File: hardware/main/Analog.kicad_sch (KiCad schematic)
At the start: 61 parts, among them J301 Overvoltage_protection, J302 Rad_sensor, J303 Mos_temp, J304 Diode_temp, U301 INA823DT, U302 INA823DT, U303 INA293A4, U304 INA293A4, U305 TL7726IDR_1

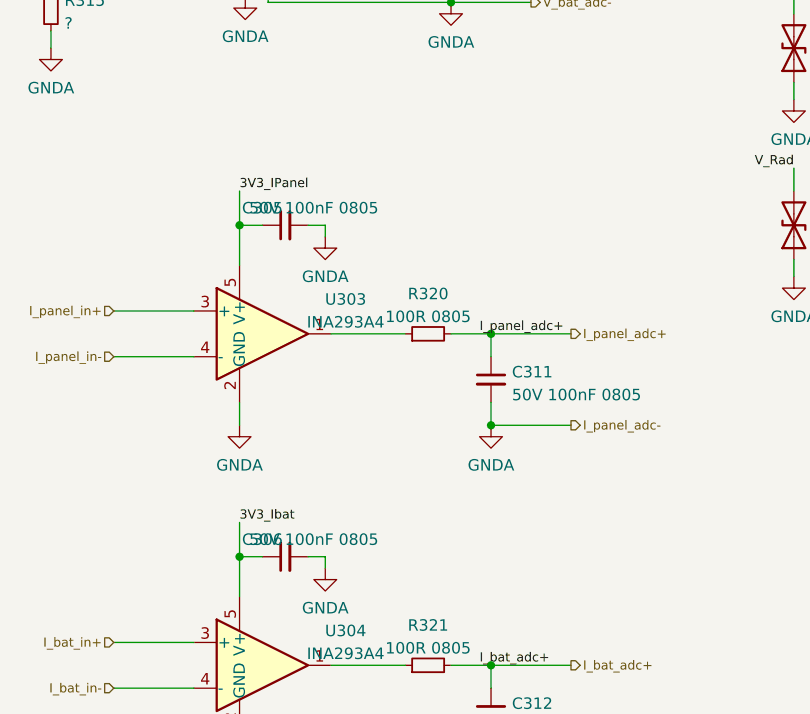
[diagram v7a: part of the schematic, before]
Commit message: Layout: Fist version of power stage
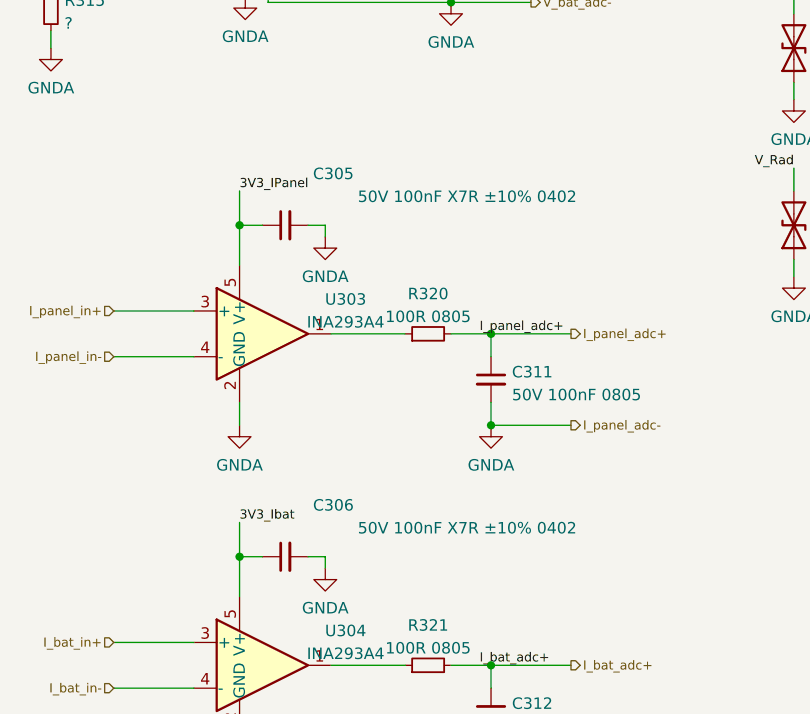
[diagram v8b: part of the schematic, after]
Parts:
- C305, C306: value 50V 100nF 0805 -> 50V 100nF X7R ±10% 0402; footprint Capacitor_SMD:C_0805_2012Metric_Pad1.18x1.45mm_HandSolder -> Capacitor_SMD:C_0402_1005Metric_Pad0.74x0.62mm_HandSolder
- JP301, JP302, JP303, JP304: footprint Jumper:SolderJumper-2_P1.3mm_Open_TrianglePad1.0x1.5mm -> Zenite:SolderJumper-2_P0.5mm_Open_TrianglePad0.5x0.5mm
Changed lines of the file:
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@@
+    (stroke (width 0) (type default) (color 0 0 0 0))
+  )
+  (wire (pts (xy 128.27 164.465) (xy 130.81 164.465))
     (stroke (width 0) (type default) (color 0 0 0 0))
   )
@@
   )
   (wire (pts (xy 135.89 164.465) (xy 137.795 164.465))
-    (stroke (width 0) (type default) (color 0 0 0 0))
-  )
-  (wire (pts (xy 128.27 164.465) (xy 130.81 164.465))
     (stroke (width 0) (type default) (color 0 0 0 0))
   )
@@
     )
     (property "Datasheet" "~" (id 3) (at 100.965 97.79 0)
+      (effects (font (size 1.27 1.27)) hide)
+    )
+    (pin "1")
+    (pin "2")
+  )
+  (symbol (lib_id "Device:C_Small") (at 133.35 127.635 90) (unit 1)
+    (in_bom yes) (on_board yes)
+    (property "Reference" "C305" (id 0) (at 140.97 121.92 90)
+      (effects (font (size 1.27 1.27)) (justify left))
+    )
+    (property "Value" "50V 100nF X7R ±10% 0402" (id 1) (at 165.735 124.46 90)
+      (effects (font (size 1.27 1.27)) (justify left))
+    )
+    (property "Footprint" "Capacitor_SMD:C_0402_1005Metric_Pad0.74x0.62mm_HandSolder" (id 2) (at 133.35 127.635 0)
+      (effects (font (size 1.27 1.27)) hide)
+    )
+    (property "Datasheet" "~" (id 3) (at 133.35 127.635 0)
       (effects (font (size 1.27 1.27)) hide)
     )
@@
     (property "Reference" "JP304" (id 0) (at 257.175 53.4502 0))
     (property "Value" "Disable_Ibat" (id 1) (at 257.175 55.9871 0))
-    (property "Footprint" "Jumper:SolderJumper-2_P1.3mm_Open_TrianglePad1.0x1.5mm" (id 2) (at 257.175 57.785 0)
+    (property "Footprint" "Zenite:SolderJumper-2_P0.5mm_Open_TrianglePad0.5x0.5mm" (id 2) (at 257.175 57.785 0)
       (effects (font (size 1.27 1.27)) hide)
     )
@@
     (pin "1")
   )
+  (symbol (lib_id "Device:C_Small") (at 133.35 164.465 90) (unit 1)
+    (in_bom yes) (on_board yes)
+    (property "Reference" "C306" (id 0) (at 140.97 158.75 90)
+      (effects (font (size 1.27 1.27)) (justify left))
+    )
+    (property "Value" "50V 100nF X7R ±10% 0402" (id 1) (at 165.735 161.29 90)
+      (effects (font (size 1.27 1.27)) (justify left))
+    )
+    (property "Footprint" "Capacitor_SMD:C_0402_1005Metric_Pad0.74x0.62mm_HandSolder" (id 2) (at 133.35 164.465 0)
+      (effects (font (size 1.27 1.27)) hide)
+    )
+    (property "Datasheet" "~" (id 3) (at 133.35 164.465 0)
+      (effects (font (size 1.27 1.27)) hide)
+    )
+    (pin "1")
+    (pin "2")
+  )
   (symbol (lib_id "power:GNDA") (at 107.315 68.58 0) (unit 1)
     (in_bom yes) (on_board yes) (fields_autoplaced)
@@
     )
     (property "Datasheet" "~" (id 3) (at 56.515 113.665 0)
-      (effects (font (size 1.27 1.27)) hide)
-    )
-    (pin "1")
-    (pin "2")
-  )
-  (symbol (lib_id "Device:C_Small") (at 133.35 127.635 90) (unit 1)
-    (in_bom yes) (on_board yes)
-    (property "Reference" "C305" (id 0) (at 130.81 125.73 90))
-    (property "Value" "50V 100nF 0805" (id 1) (at 136.525 125.73 90))
-    (property "Footprint" "Capacitor_SMD:C_0805_2012Metric_Pad1.18x1.45mm_HandSolder" (id 2) (at 133.35 127.635 0)
-      (effects (font (size 1.27 1.27)) hide)
-    )
-    (property "Datasheet" "~" (id 3) (at 133.35 127.635 0)
       (effects (font (size 1.27 1.27)) hide)
     )
@@
     (property "Reference" "JP301" (id 0) (at 257.175 36.3052 0))
     (property "Value" "Disable_Vpanel" (id 1) (at 257.175 38.8421 0))
-    (property "Footprint" "Jumper:SolderJumper-2_P1.3mm_Open_TrianglePad1.0x1.5mm" (id 2) (at 257.175 40.64 0)
+    (property "Footprint" "Zenite:SolderJumper-2_P0.5mm_Open_TrianglePad0.5x0.5mm" (id 2) (at 257.175 40.64 0)
       (effects (font (size 1.27 1.27)) hide)
     )
@@
     (property "Reference" "JP302" (id 0) (at 257.175 42.0202 0))
     (property "Value" "Disable_Vbat" (id 1) (at 257.175 44.5571 0))
-    (property "Footprint" "Jumper:SolderJumper-2_P1.3mm_Open_TrianglePad1.0x1.5mm" (id 2) (at 257.175 46.355 0)
+    (property "Footprint" "Zenite:SolderJumper-2_P0.5mm_Open_TrianglePad0.5x0.5mm" (id 2) (at 257.175 46.355 0)
       (effects (font (size 1.27 1.27)) hide)
     )
@@
     (pin "2")
   )
-  (symbol (lib_id "Device:C_Small") (at 133.35 164.465 90) (unit 1)
-    (in_bom yes) (on_board yes)
-    (property "Reference" "C306" (id 0) (at 130.81 162.56 90))
-    (property "Value" "50V 100nF 0805" (id 1) (at 136.525 162.56 90))
-    (property "Footprint" "Capacitor_SMD:C_0805_2012Metric_Pad1.18x1.45mm_HandSolder" (id 2) (at 133.35 164.465 0)
-      (effects (font (size 1.27 1.27)) hide)
-    )
-    (property "Datasheet" "~" (id 3) (at 133.35 164.465 0)
-      (effects (font (size 1.27 1.27)) hide)
-    )
-    (pin "1")
-    (pin "2")
-  )
   (symbol (lib_id "Device:Thermistor_NTC") (at 27.305 80.01 0) (unit 1)
     (in_bom yes) (on_board yes)
@@
     (property "Reference" "JP303" (id 0) (at 257.175 47.7352 0))
     (property "Value" "Disabel_Ipanel" (id 1) (at 257.175 50.2721 0))
-    (property "Footprint" "Jumper:SolderJumper-2_P1.3mm_Open_TrianglePad1.0x1.5mm" (id 2) (at 257.175 52.07 0)
-      (effects (font (size 1.27 1.27)) hide)
-    )
+    (property "Footprint" "Zenite:SolderJumper-2_P0.5mm_Open_TrianglePad0.5x0.5mm" (id 2) (at 257.175 52.07 0)
+      (effects (font (size 1.27 1.27)) hide)
+    )
